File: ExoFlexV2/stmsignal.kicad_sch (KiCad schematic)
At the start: 5 parts

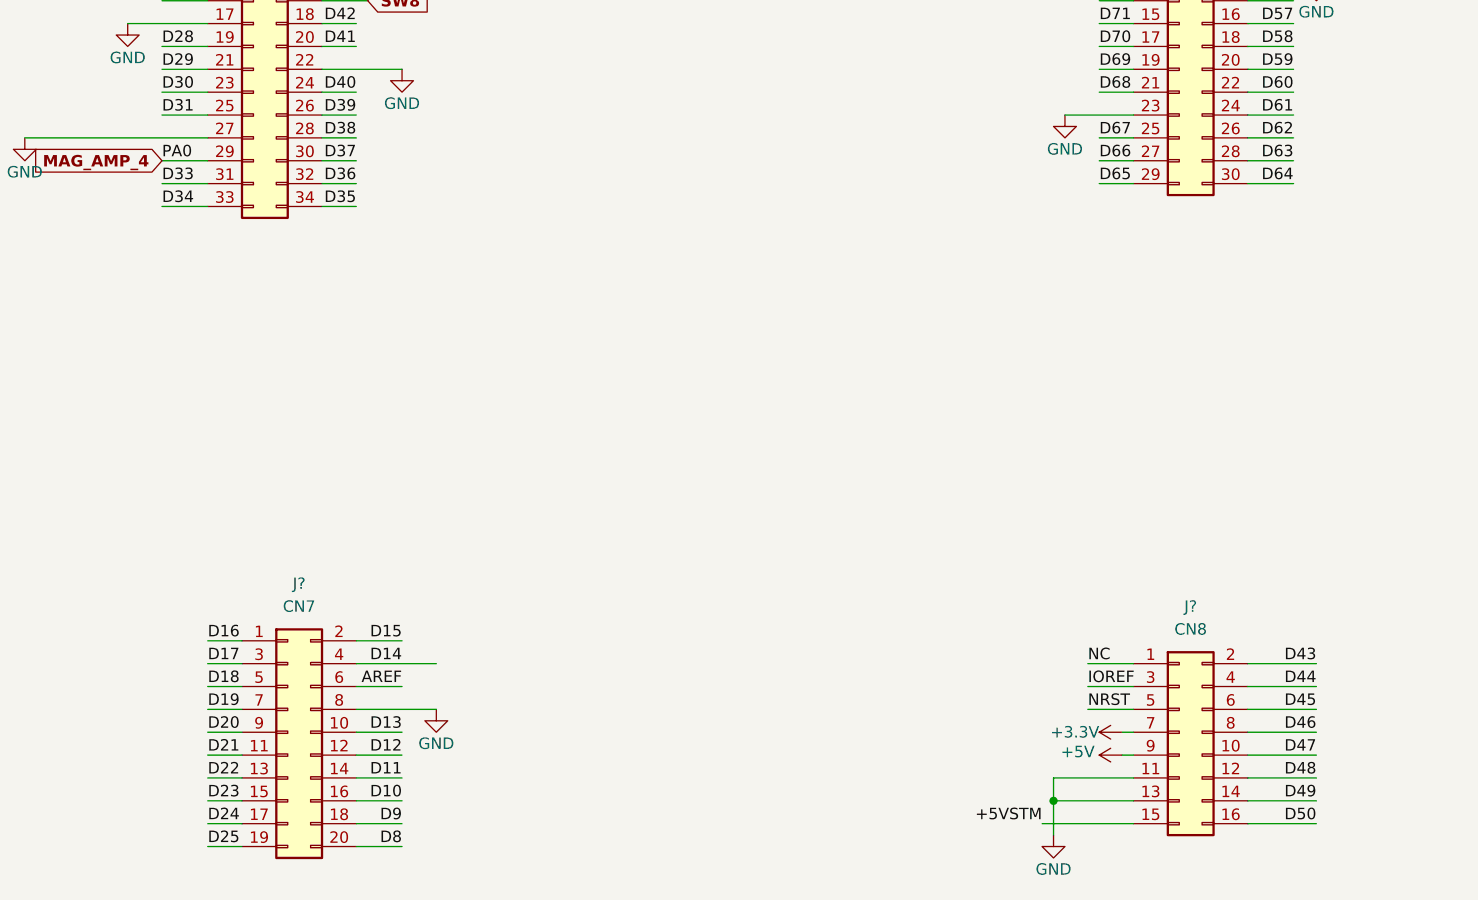
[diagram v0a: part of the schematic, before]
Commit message: Schematic structure
Ajout des Encodeur magnétique et load cells, début de circuit de comparateurs
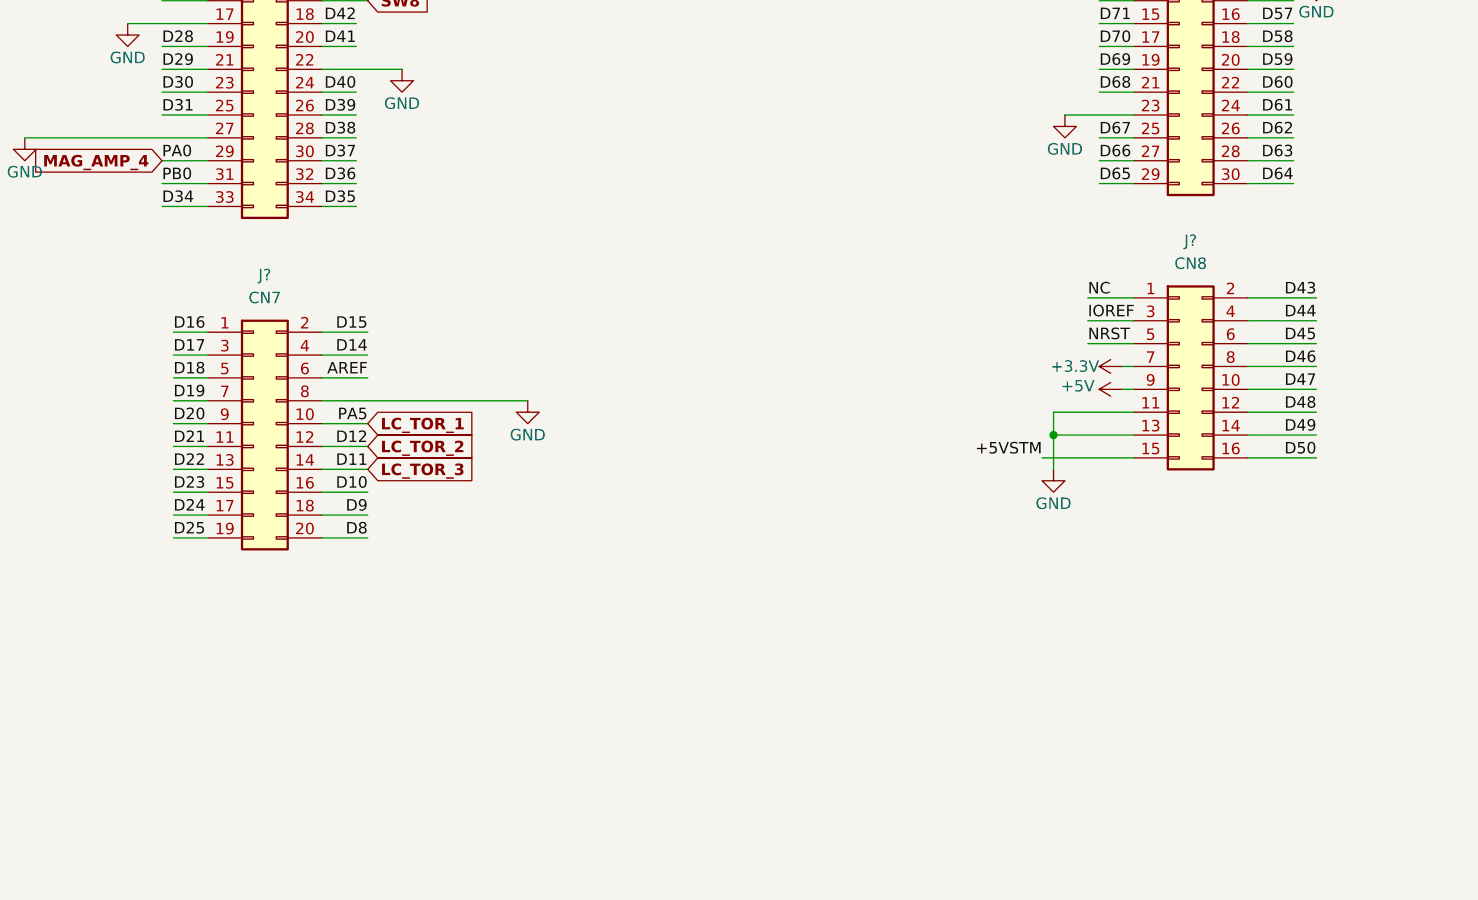
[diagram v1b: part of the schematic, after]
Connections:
- net D11 renamed LC_TOR_3
- net D12 renamed LC_TOR_2
- net D13 renamed LC_TOR_1
- net D33 renamed PB0
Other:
- moved on the sheet: J?

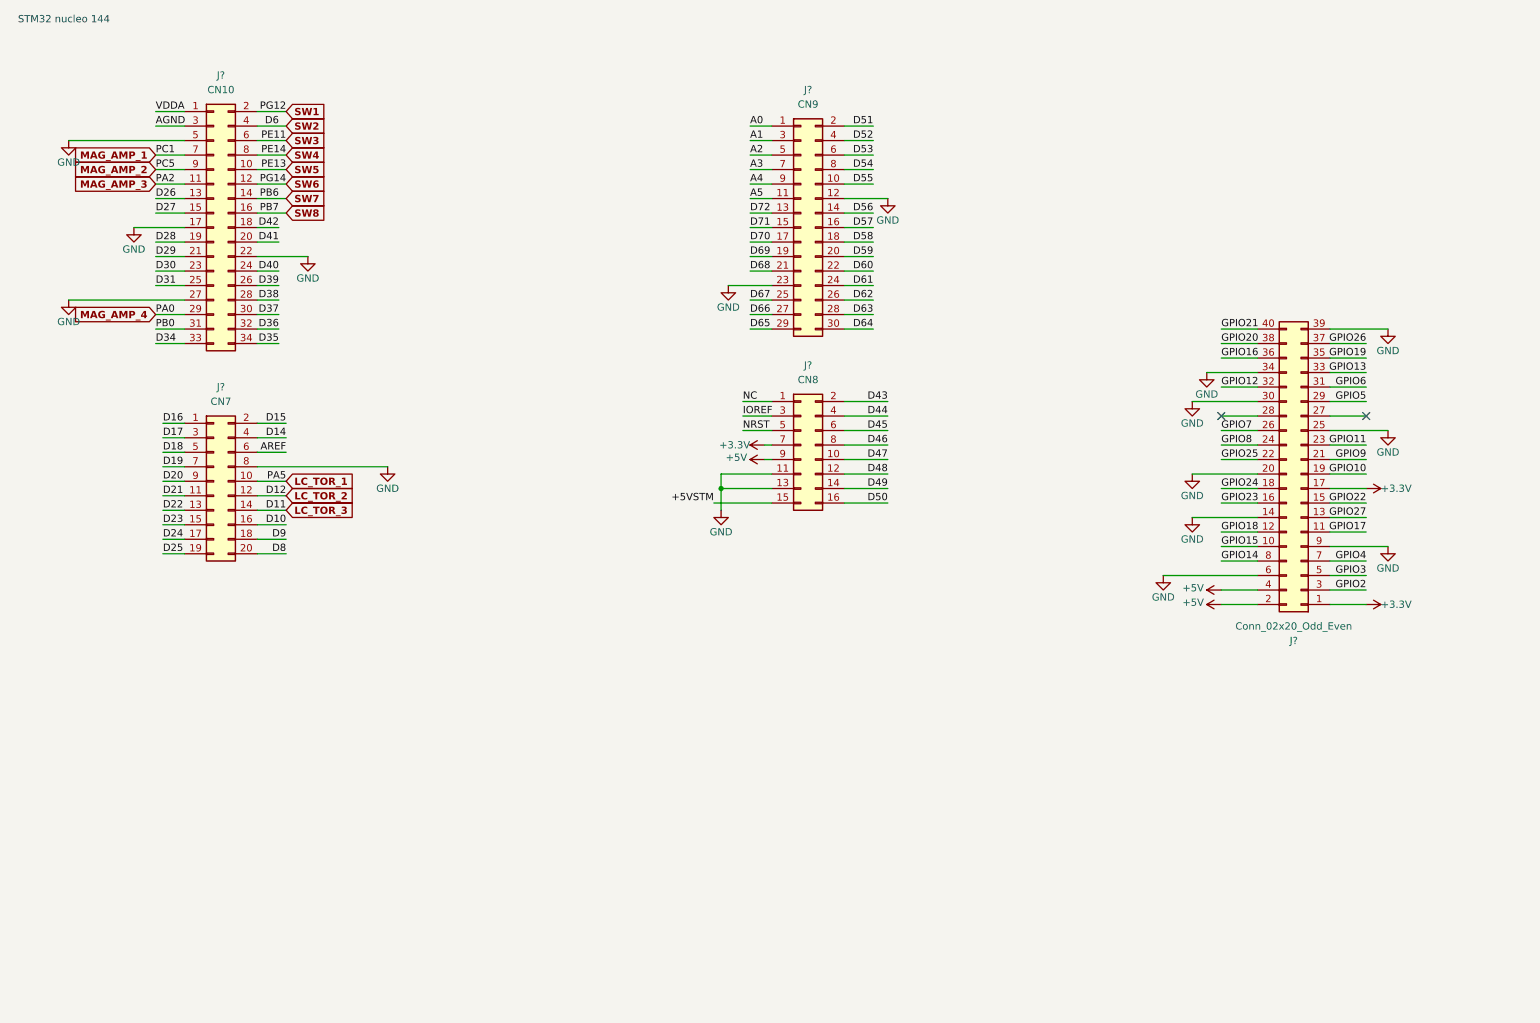
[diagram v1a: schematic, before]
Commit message: Many changes
Debouncing, power protection, potentiometer limits, etc.
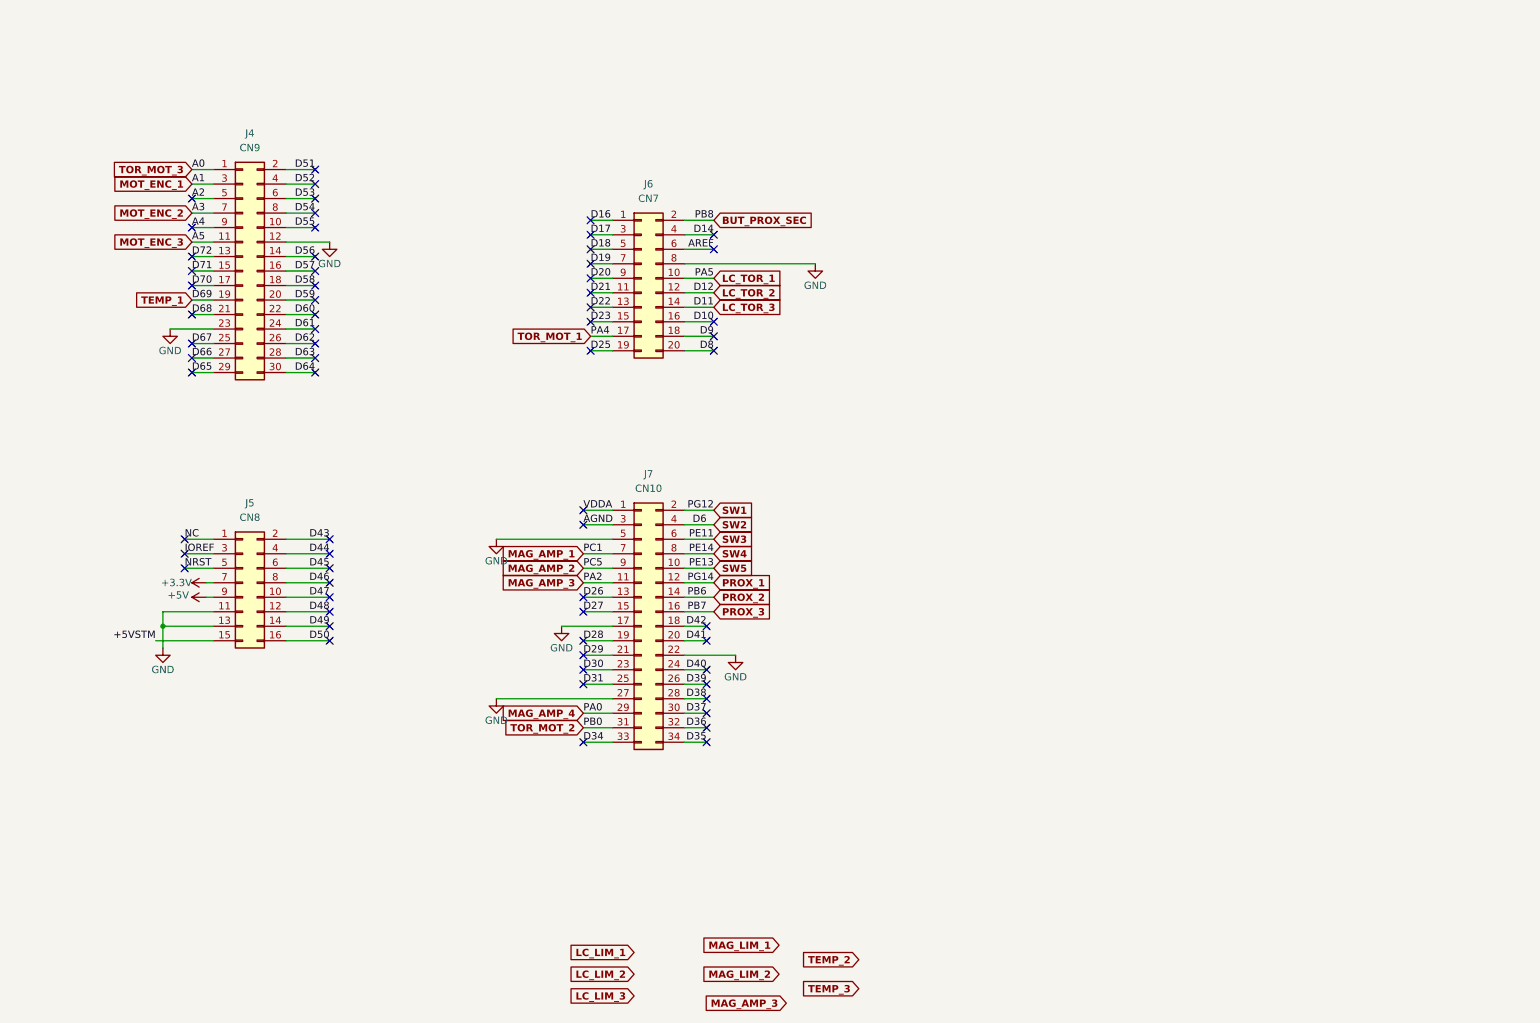
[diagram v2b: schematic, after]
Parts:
- removed J?: Conn_02x20_Odd_Even, symbol Connector_Generic:Conn_02x20_Odd_Even
- gave numbers to parts that had none: 4
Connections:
- net A0 renamed TOR_MOT_3
- net A1 renamed MOT_ENC_1
- net A3 renamed MOT_ENC_2
- net A5 renamed MOT_ENC_3
- net D15 renamed BUT_PROX_SEC
- net D24 renamed TOR_MOT_1
- net D69 renamed TEMP_1
- net PB0 renamed TOR_MOT_2
- net SW6 renamed PROX_1
- net SW7 renamed PROX_2
- net SW8 renamed PROX_3
- no-connect marks 2 -> 65
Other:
- note removed: "STM32 nucleo 144"
- moved on the sheet: J4, J5, J6, J7

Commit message: Placement
Début du placement et modification d'après dernier review
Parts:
- renumbered J5 to J4, J4 to J5
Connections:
- net +5VSTM is gone; now on net VDD: J4.15 (Pin_15)
- net BUT_PROX_SEC is gone; now on net PROX_1: J6.2 (Pin_2)
- net D10 is gone; now on net PROX_3: J6.16 (Pin_16)
- net D14 is gone; now on net PROX_2: J6.4 (Pin_4)
- net LC_LIM_1: now also J6.17 (Pin_17)
- net LC_LIM_2: now also J7.31 (Pin_31)
- net LC_LIM_3: now also J5.1 (Pin_1)
- net MAG_LIM_1: now also J5.3 (Pin_3)
- net MAG_LIM_2: now also J5.7 (Pin_7)
- net MOT_ENC_1: no longer J5.3 (Pin_3)
- net MOT_ENC_2: no longer J5.7 (Pin_7)
- net MOT_ENC_3: no longer J5.11 (Pin_11)
- net PROX_1: no longer J7.12 (Pin_12)
- net PROX_2: no longer J7.14 (Pin_14)
- net PROX_3: no longer J7.16 (Pin_16)
- net TOR_MOT_1: no longer J6.17 (Pin_17)
- net TOR_MOT_2: no longer J7.31 (Pin_31)
- net TOR_MOT_3: no longer J5.1 (Pin_1)
- net +5V renamed VDD
- net D8 renamed PROX_5
- net D9 renamed PROX_4
- net SW1 renamed SWMAX1
- net SW2 renamed SWMIN1
- net SW3 renamed SWMAX2
- net SW4 renamed SWMIN2
- net SW5 renamed SWMAX3
- new net MAG_LIM_3: J5.11 (Pin_11)
- new net SWMAX4: J7.14 (Pin_14)
- new net SWMAX5: J7.16 (Pin_16)
- new net SWMIN3: J7.12 (Pin_12)
- no-connect marks 65 -> 67
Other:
- moved on the sheet: J4, J5, J6, J7
